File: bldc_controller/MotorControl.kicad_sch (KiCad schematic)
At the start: 0 parts

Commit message: some progress
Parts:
- added C35, C36, C37: 1n, symbol Device:C_Small
- added C38: 100n X7R 16V, symbol Device:C_Small
- added C39: 100n X7R 100V, symbol Device:C_Small
- added C40, C42: 1u X7R 25V, symbol Device:C
- added C41: 47n X7R 100V, symbol Device:C_Small
- added C43: 1u X7R 16V, symbol Device:C
- added C44: 470n X7R 100V, symbol Device:C_Small
- added R29, R33: 2k, symbol Device:R
- added R30, R31, R32: 22R, symbol Device:R_Small
- added U6: DRV8353FS, Package_DFN_QFN:HVQFN-40-1EP_6x6mm_P0.5mm_EP4.1x4.1mm_ThermalVias, symbol 0_motor_driver:DRV8353FS
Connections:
- new net +3V3: C38.1, R29.1, R33.1, U6.24 (VREF)
- new net +VBAT: C39.1, C40.1, C44.1, U6.3 (VM), U6.4 (VDRAIN)
- new net -VBAT: C39.2, C42.2, C43.2, C44.2, U6.25 (AGND), U6.39 (GND)
- new net CPH: C41.1, U6.2 (CPH)
- new net CPL: C41.2, U6.1 (CPL)
- new net DRV_CS: U6.30 (nSCS)
- new net DRV_MISO: R29.2, U6.27 (SDO)
- new net DRV_MOSI: U6.28 (SDI)
- new net DRV_SCLK: U6.29 (SCLK)
- new net DVDD: C43.1, U6.38 (DVDD)
- new net FILTER_SOA: C37.2, R30.1
- new net FILTER_SOB: C36.2, R31.1
- new net FILTER_SOC: C35.2, R32.1
- new net GHA: U6.6 (GHA)
- new net GHB: U6.15 (GHB)
- new net GHC: U6.16 (GHC)
- new net GLA: U6.8 (GLA)
- new net GLB: U6.13 (GLB)
- new net GLC: U6.18 (GLC)
- new net GND: C35.1, C36.1, C37.1, C38.2, U6.41 (EP)
- new net MOTOR_ENABLE: U6.31 (ENABLE)
- new net MOTOR_FAULT: R33.2, U6.26 (nFAULT)
- new net MOTOR_HIZ: U6.33 (INLA), U6.35 (INLB), U6.37 (INLC)
- new net PWM_PHASEA: U6.32 (INHA)
- new net PWM_PHASEB: U6.34 (INHB)
- new net PWM_PHASEC: U6.36 (INHC)
- new net SA_N: U6.10 (SNA)
- new net SA_P: U6.9 (SPA)
- new net SB_N: U6.11 (SNB)
- new net SB_P: U6.12 (SPB)
- new net SC_N: U6.20 (SNC)
- new net SC_P: U6.19 (SPC)
- new net SHA: U6.7 (SHA)
- new net SHB: U6.14 (SHB)
- new net SHC: U6.17 (SHC)
- new net SOA: R30.2, U6.23 (SOA)
- new net SOB: R31.2, U6.22 (SOB)
- new net SOC: R32.2, U6.21 (SOC)
- new net VCP: C40.2, U6.5 (VCP)
- new net VGLS: C42.1, U6.40 (VGLS)
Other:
- added sheet Three Phase Inverter (MotorControl_ThreePhaseInverter.kicad_sch)
- note added: "13"
- note added: "Single supply mode: VDRAIN = VM"
- company: (none) -> EPFL Xplore
- title: (none) -> Motor Control Gate Driver

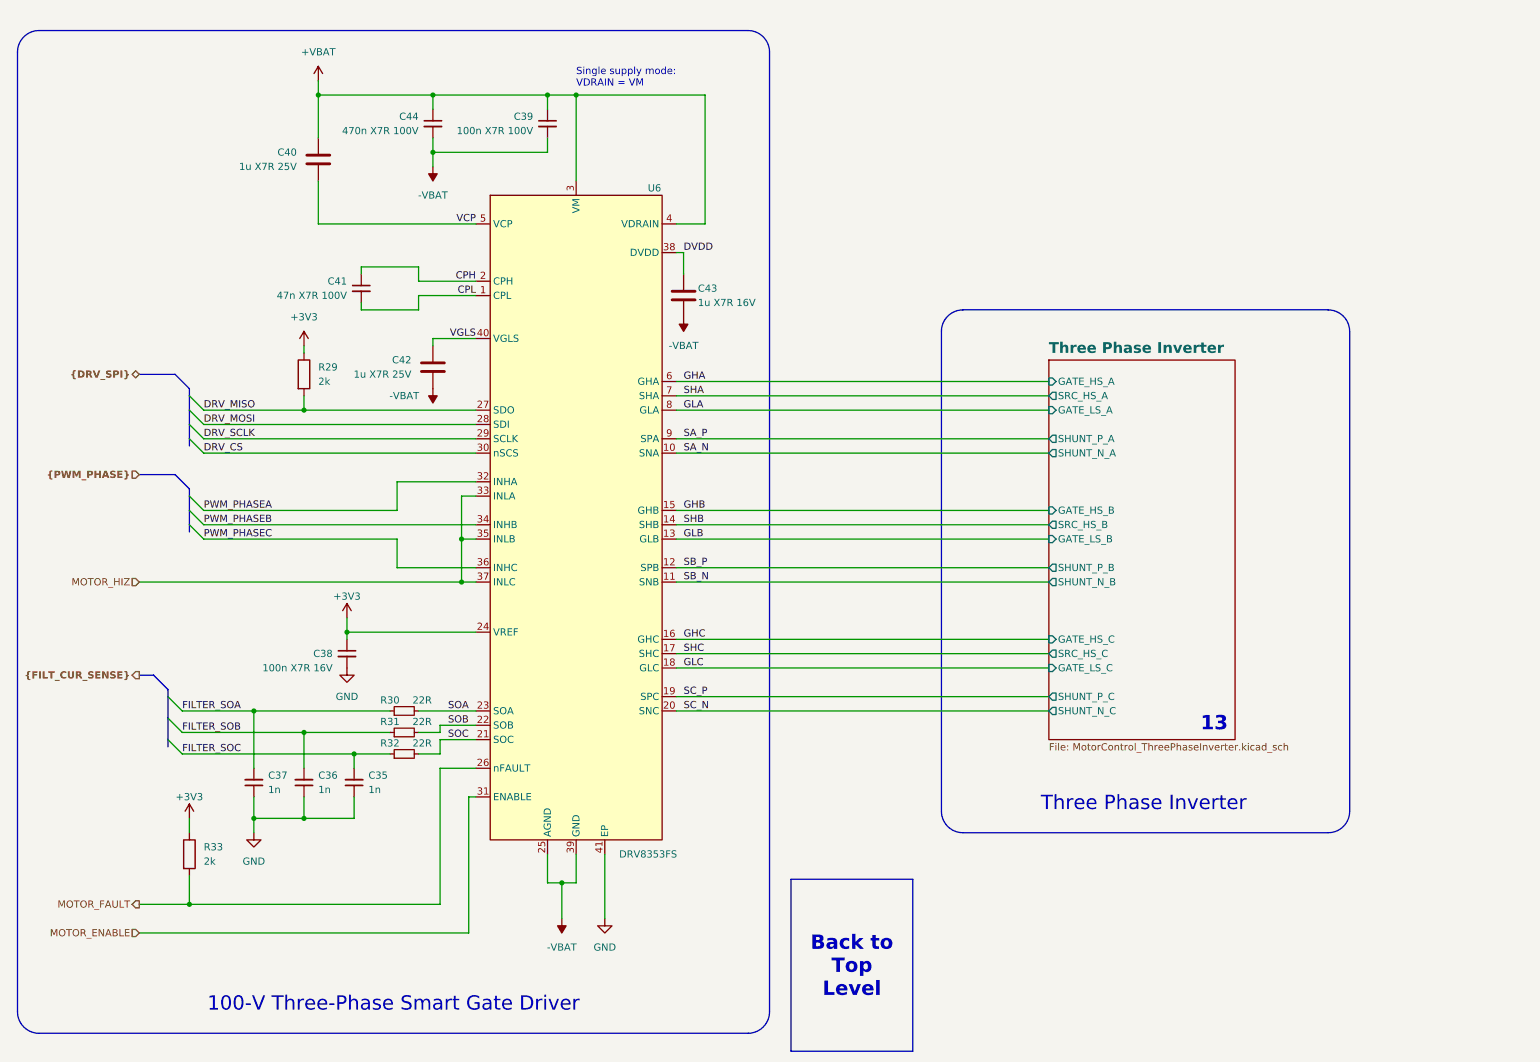
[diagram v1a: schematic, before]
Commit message: added temporary footprints and deleted extra files
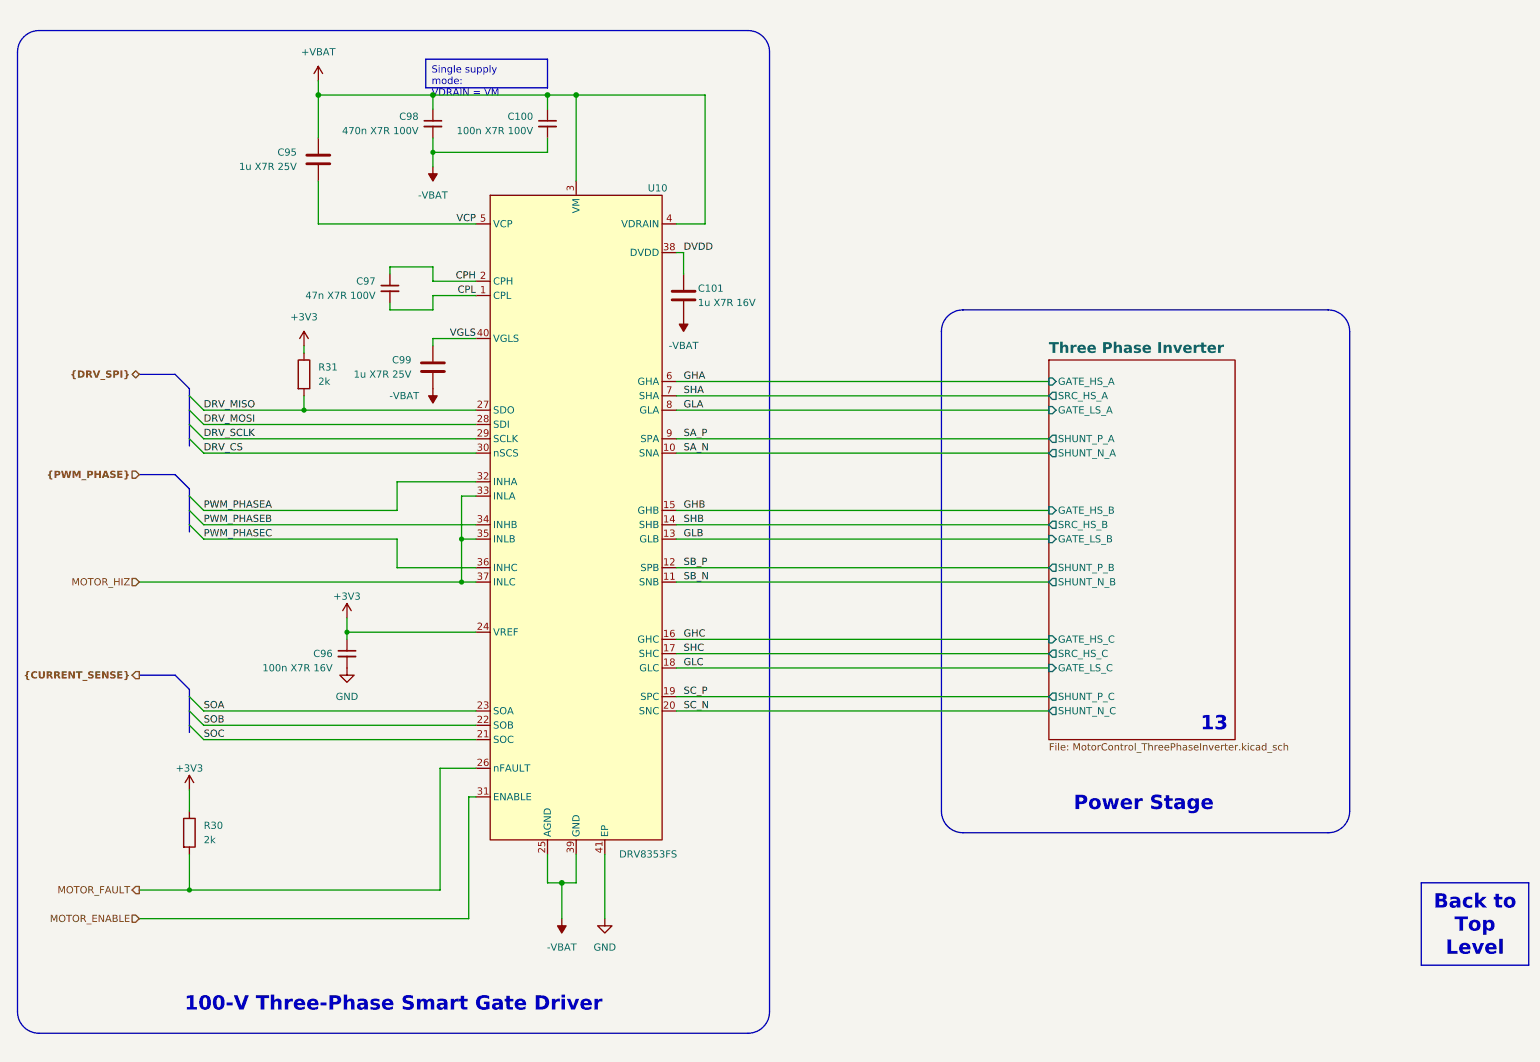
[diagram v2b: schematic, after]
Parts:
- removed C35, C36, C37: 1n, symbol Device:C_Small
- removed R30, R31, R32: 22R, symbol Device:R_Small
- C101: renamed from C43; footprint (none) -> Capacitor_SMD:C_0402_1005Metric
- C95: renamed from C40; footprint (none) -> Capacitor_SMD:C_0402_1005Metric
- C96: renamed from C38; footprint (none) -> Capacitor_SMD:C_0402_1005Metric
- C97: renamed from C41; footprint (none) -> Capacitor_SMD:C_0402_1005Metric
- C98: renamed from C44; footprint (none) -> Capacitor_SMD:C_0402_1005Metric
- C99: renamed from C42; footprint (none) -> Capacitor_SMD:C_0402_1005Metric
- R30: renamed from R33; footprint (none) -> Resistor_SMD:R_0402_1005Metric
- R31: renamed from R29; footprint (none) -> Resistor_SMD:R_0402_1005Metric
- renumbered C39 to C100, U6 to U10
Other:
- note removed: "Single supply mode: VDRAIN = VM"
- moved on the sheet: C97, R30

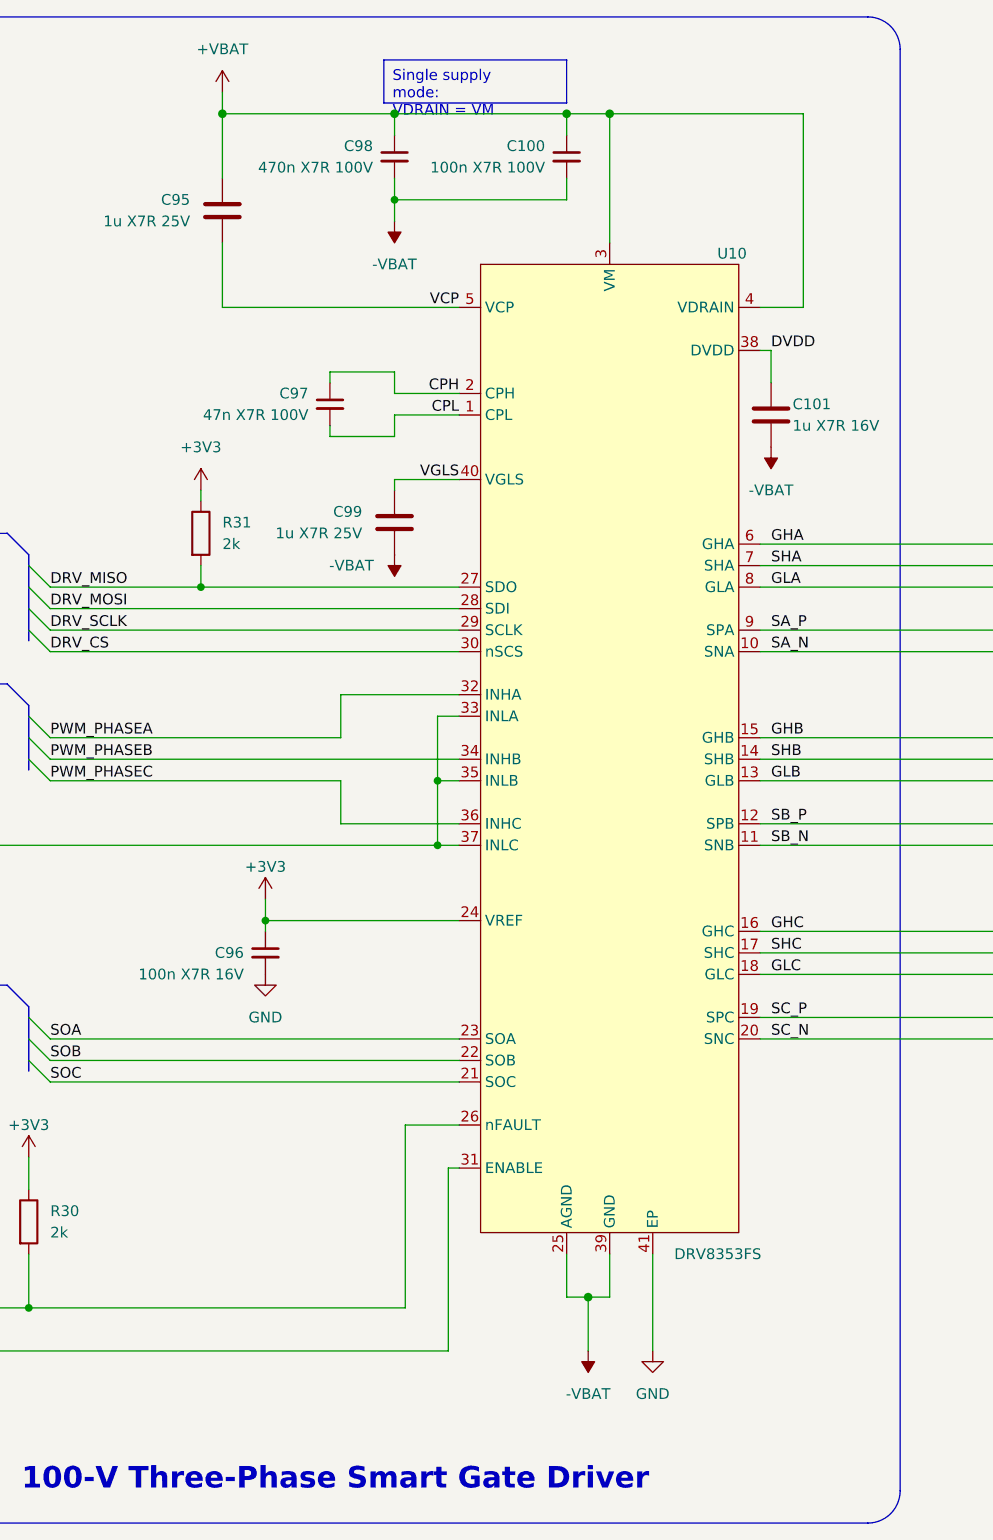
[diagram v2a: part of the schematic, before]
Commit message: added IPC-7351 compliant footprints and started routing
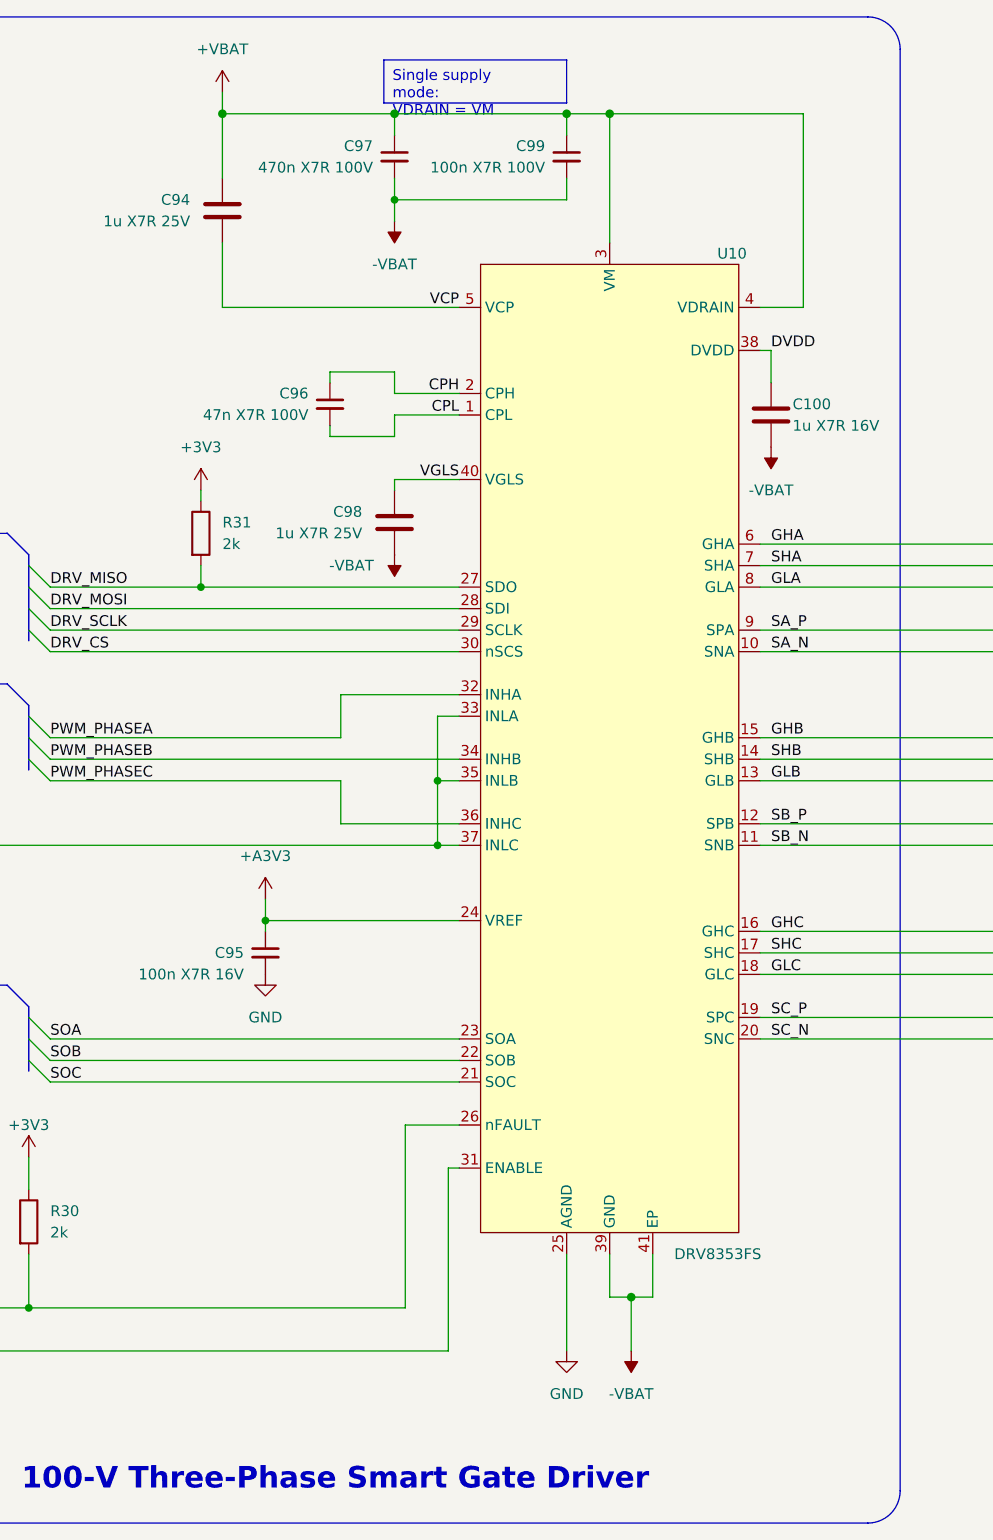
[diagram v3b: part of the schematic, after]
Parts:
- removed C100: 100n X7R 100V, symbol Device:C_Small
- added C99: 100n X7R 100V, 0_capacitor_smd:C_0402_1005_DensityHigh, symbol Device:C_Small
- C100: renamed from C101; footprint Capacitor_SMD:C_0402_1005Metric -> 0_capacitor_smd:C_0402_1005_DensityHigh
- C94: renamed from C95; footprint Capacitor_SMD:C_0402_1005Metric -> 0_capacitor_smd:C_0402_1005_DensityHigh
- C95: renamed from C96; footprint Capacitor_SMD:C_0402_1005Metric -> 0_capacitor_smd:C_0402_1005_DensityHigh
- C96: renamed from C97; footprint Capacitor_SMD:C_0402_1005Metric -> 0_capacitor_smd:C_0402_1005_DensityHigh
- C97: renamed from C98; footprint Capacitor_SMD:C_0402_1005Metric -> 0_capacitor_smd:C_0402_1005_DensityHigh
- C98: renamed from C99; footprint Capacitor_SMD:C_0402_1005Metric -> 0_capacitor_smd:C_0402_1005_DensityHigh
- R30, R31: footprint Resistor_SMD:R_0402_1005Metric -> 0_resistor_smd:R_0402_1005_DensityHigh
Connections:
- net +3V3: no longer C95.1, U10.24 (VREF)
- net +VBAT: now also C99.1
- net -VBAT: now also U10.41 (EP), C99.2; no longer U10.25 (AGND)
- net GND: now also U10.25 (AGND); no longer U10.41 (EP)
- new net +A3V3: C95.1, U10.24 (VREF)

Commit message: some progress on the pcb
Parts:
- C94, C99: footprint 0_capacitor_smd:C_0402_1005_DensityHigh -> 0_capacitor_smd:C_0402_1005_DensitySpaced
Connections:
- net -VBAT is gone; now on net GND: C100.2, C97.2, C98.2, C99.2, U10.39 (GND), U10.41 (EP)
